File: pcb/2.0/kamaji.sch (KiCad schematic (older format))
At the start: 43 parts, among them J1 RJ10, J2 RJ10, J3 RJ10, J4 RJ10, J5 RJ10, J6 ICSP, J7 USB_B, J8 USB_A, Q1 2N3904, Q2 IRL540N, SW1 SW_Push, SW2 SW_Push, SW3 SW_Push, U1 ATMEGA32U4-AU, Y1 16MHz

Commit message: get gid of 2 nested sheets
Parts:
- added DS1: LCD12864B, kamaji:LCD12864, symbol LCD12864B
- added Q3: IRL540N, TO_SOT_Packages_THT:TO-220-3_Horizontal, symbol IRLIZ44N
- added R20, R25, R26: 10K, symbol R
- added R21, R22, R23, R24: 200R, symbol R
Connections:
- net labels added: DUMMY_EN, LCD_CS, LCD_RST
- no-connect marks 4 -> 6
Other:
- note added: "Dummy load to make sure\npowerbanks don't shut off\npower due to low current"
- note added: "ST7920-based LCD\ndisplay in serial mode"
- moved on the sheet: R8, SW1, SW2, SW3

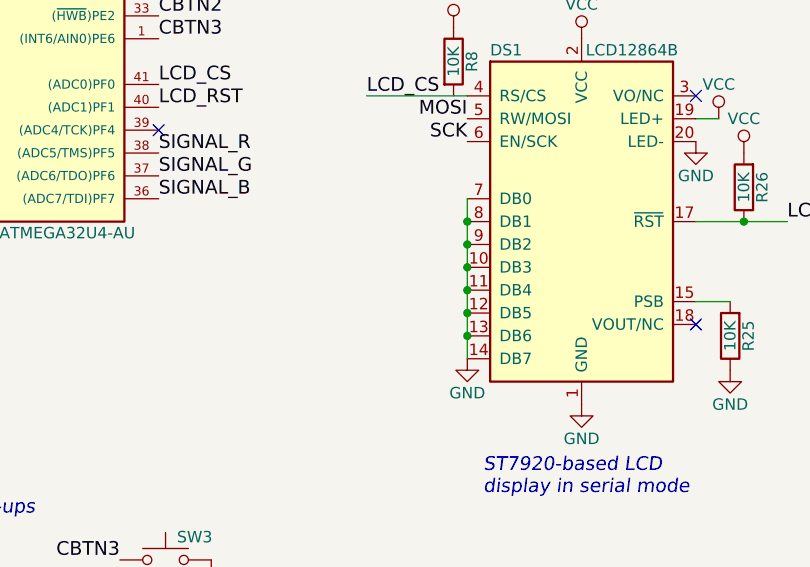
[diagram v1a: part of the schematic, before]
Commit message: minor schamatic changes
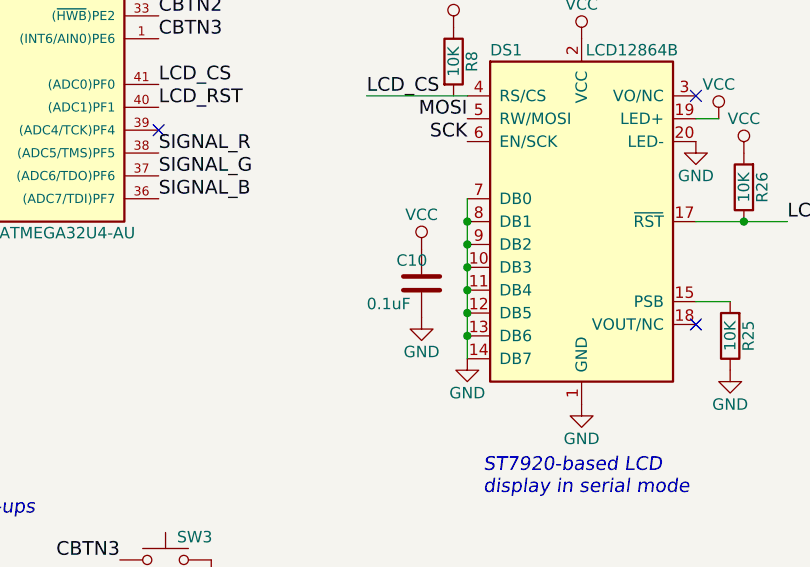
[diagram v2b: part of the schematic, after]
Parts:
- added C10: 0.1uF, symbol C

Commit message: start mapping components to footprints
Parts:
- C1, C10, C2, C3, C4, C5, C6: footprint (none) -> Capacitors_SMD:C_1206_HandSoldering
- J1, J2, J3, J4, J5: footprint (none) -> kamaji:RJ10
- J6: footprint (none) -> Connectors_IDC:IDC-Header_2x03_Pitch2.54mm_Straight
- J7: footprint (none) -> Connectors:USB_B
- J8: footprint (none) -> Connectors:USB_A
- JP1, JP2, JP3: footprint (none) -> Socket_Strips:Socket_Strip_Straight_1x02_Pitch2.54mm
- LS1: footprint (none) -> kamaji:buzzer_30x17
- R1, R10, R11, R12, R13, R14, R15, R2, R20, R21, R22, R23, R24, R25, R26, R3, R4, R5, R6, R7, R8, R9: footprint (none) -> Resistors_SMD:R_1206_HandSoldering

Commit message: finish mapping components to footprints
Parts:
- D1: footprint (none) -> kamaji:LED_RGB_common_cathode_5mm
- F1: footprint (none) -> Resistors_SMD:R_1812_HandSoldering
- RV2: footprint (none) -> kamaji:Potentiometer_Wheel_16mm
- SW1, SW2, SW3: footprint (none) -> Buttons_Switches_THT:SW_PUSH-12mm
- Y1: footprint (none) -> Crystals:Crystal_HC49-U_Vertical
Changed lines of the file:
@@
 F 0 "Y1" H 1300 2130 50  0000 C CNN
 F 1 "16MHz" H 1300 1830 50  0000 C CNN
-F 2 "" H 1300 1980 50  0001 C CNN
+F 2 "Crystals:Crystal_HC49-U_Vertical" H 1300 1980 50  0001 C CNN
 F 3 "" H 1300 1980 50  0001 C CNN
 	1    1300 1980
@@
 F 0 "SW1" H 1400 6060 50  0000 L CNN
 F 1 "SW_Push" H 1350 5900 50  0001 C CNN
-F 2 "" H 1350 6160 50  0001 C CNN
+F 2 "Buttons_Switches_THT:SW_PUSH-12mm" H 1350 6160 50  0001 C CNN
 F 3 "" H 1350 6160 50  0001 C CNN
 	1    1350 5960
@@
 F 0 "SW2" H 2630 6060 50  0000 L CNN
 F 1 "SW_Push" H 2580 5900 50  0001 C CNN
-F 2 "" H 2580 6160 50  0001 C CNN
+F 2 "Buttons_Switches_THT:SW_PUSH-12mm" H 2580 6160 50  0001 C CNN
 F 3 "" H 2580 6160 50  0001 C CNN
 	1    2580 5960
@@
 F 0 "SW3" H 3810 6060 50  0000 L CNN
 F 1 "SW_Push" H 3760 5900 50  0001 C CNN
-F 2 "" H 3760 6160 50  0001 C CNN
+F 2 "Buttons_Switches_THT:SW_PUSH-12mm" H 3760 6160 50  0001 C CNN
 F 3 "" H 3760 6160 50  0001 C CNN
 	1    3760 5960
@@
 F 0 "F1" V 8720 4950 50  0000 C CNN
 F 1 "1A" V 8565 4950 50  0000 C CNN
-F 2 "" V 8570 4950 50  0001 C CNN
+F 2 "Resistors_SMD:R_1812_HandSoldering" V 8570 4950 50  0001 C CNN
 F 3 "" H 8640 4950 50  0001 C CNN
 	1    8640 4950
@@
 F 0 "D1" H 8500 3660 50  0000 C CNN
 F 1 "LED_CRGB" H 8500 2940 50  0000 C CNN
-F 2 "" H 8500 3240 50  0001 C CNN
+F 2 "kamaji:LED_RGB_common_cathode_5mm" H 8500 3240 50  0001 C CNN
 F 3 "" H 8500 3240 50  0001 C CNN
 	1    8500 3290
@@
 F 0 "RV2" V 9870 1710 50  0000 C CNN
 F 1 "VOLUME" V 10070 1720 50  0000 C CNN
-F 2 "" H 9880 1720 50  0001 C CNN
+F 2 "kamaji:Potentiometer_Wheel_16mm" H 9880 1720 50  0001 C CNN
 F 3 "" H 9880 1720 50  0001 C CNN
 	1    9880 1720

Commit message: test point, 6th player socket
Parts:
- removed D1: LED_CRGB, kamaji:LED_RGB_common_cathode_5mm, symbol LED_CRGB
- removed JP1: Jumper, Socket_Strips:Socket_Strip_Straight_1x02_Pitch2.54mm, symbol Jumper
- removed R11, R12: 220R, Resistors_SMD:R_1206_HandSoldering, symbol R
- added J10: TEST_5V, Measurement_Points:Test_Point_2Pads, symbol TEST_2P
- added J6: RJ10, kamaji:RJ10, symbol RJ10
- added J9: TEST_28V, Measurement_Points:Test_Point_2Pads, symbol TEST_2P
- renumbered J6 to ICSP1
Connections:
- net labels added: PBTN6, PLED6
- wire segments 51 -> 52
- no-connect marks 6 -> 4
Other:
- note removed: "Break for current\nmeasurement"
- note removed: "Signal LED"
- moved on the sheet: F1, J1, J2, J3, J4, J5, R4, R5, R6, R7, R9

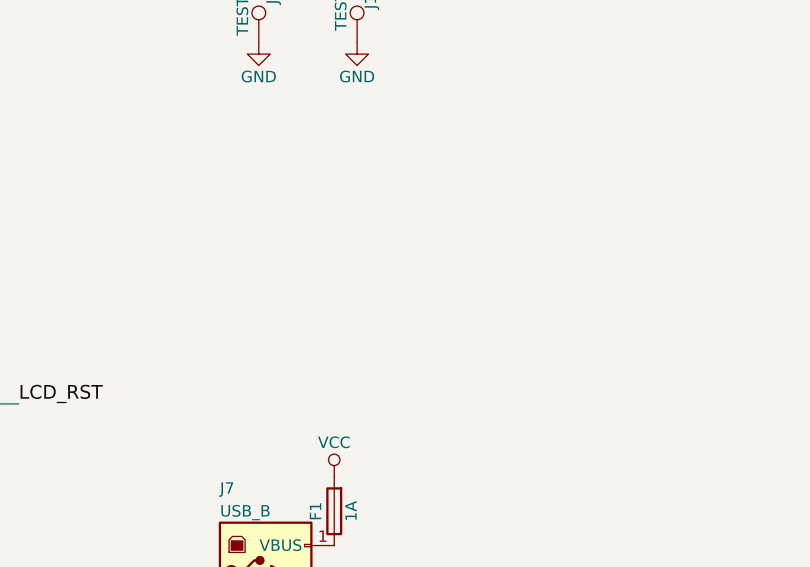
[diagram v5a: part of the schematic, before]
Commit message: place the RJ10 sockets on the PCB
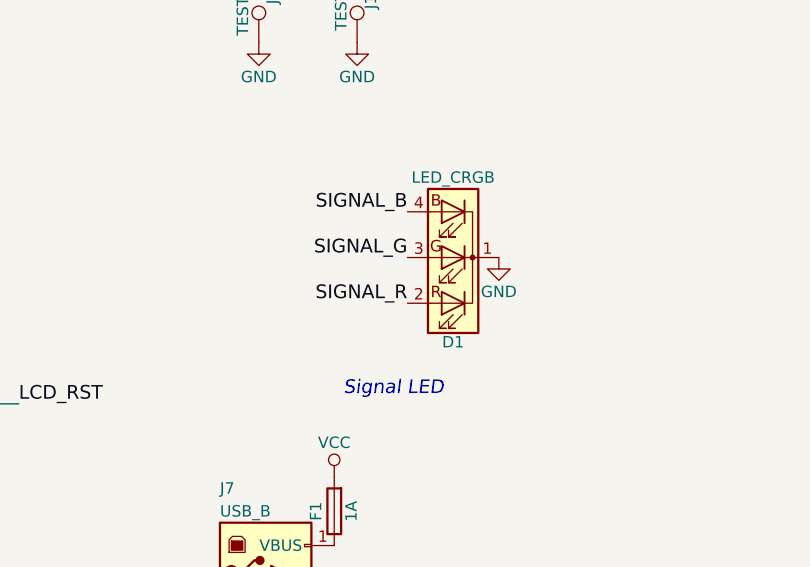
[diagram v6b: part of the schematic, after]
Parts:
- added D1: LED_CRGB, kamaji:LED_RGB_common_cathode_5mm, symbol LED_CRGB
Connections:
- net GND: now also D1.1 (K)
- net SIGNAL_B: now also D1.4 (BA)
- net SIGNAL_G: now also D1.3 (GA)
- net SIGNAL_R: now also D1.2 (RA)
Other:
- note added: "Signal LED"

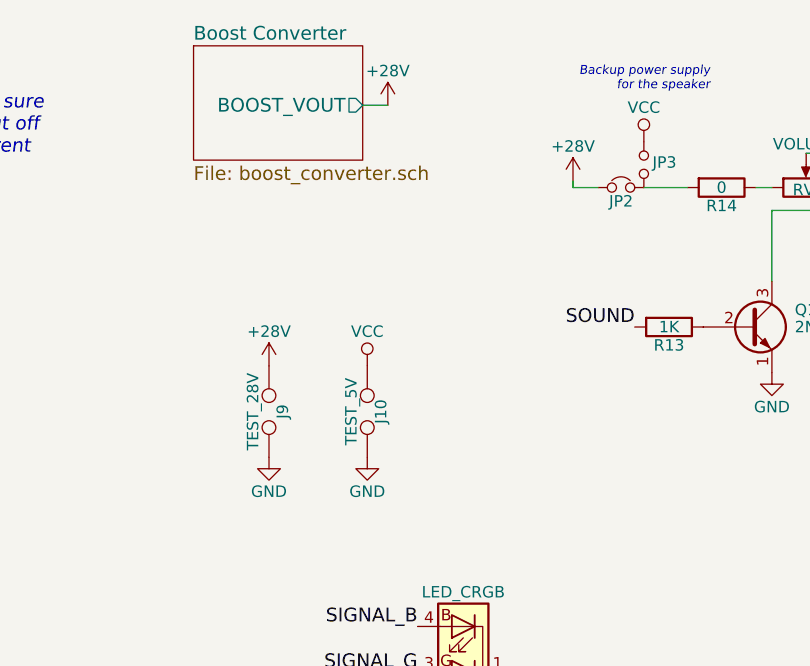
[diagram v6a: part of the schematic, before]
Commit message: roughly place components on the PCB
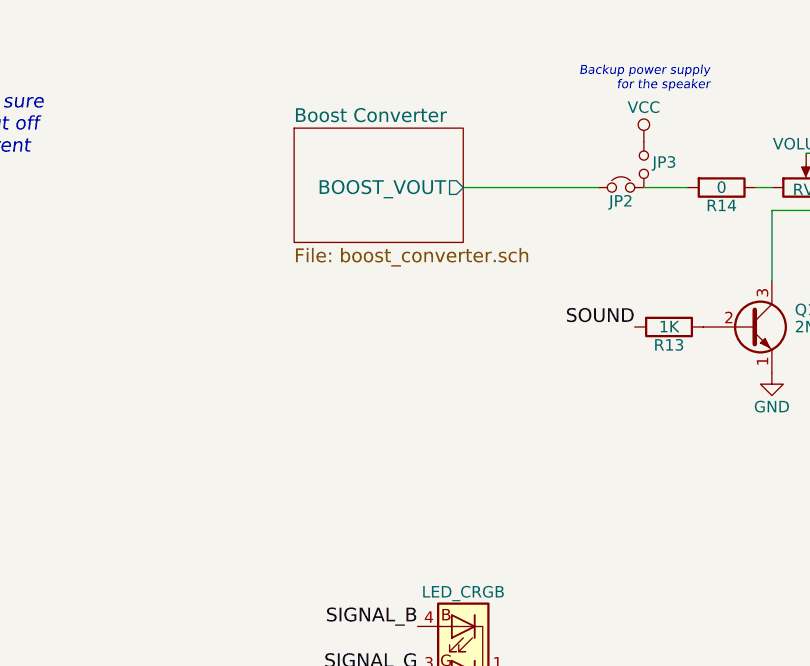
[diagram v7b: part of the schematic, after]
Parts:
- removed J10: TEST_5V, Measurement_Points:Test_Point_2Pads, symbol TEST_2P
- removed J9: TEST_28V, Measurement_Points:Test_Point_2Pads, symbol TEST_2P
- R21, R22, R23, R24: footprint Resistors_SMD:R_1206_HandSoldering -> Resistors_THT:R_Axial_DIN0207_L6.3mm_D2.5mm_P10.16mm_Horizontal
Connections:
- net +28V renamed Boost Converter/BOOST_VOUT
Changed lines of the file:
@@
-	1    0    0    -1
-$EndComp
-$Sheet
-S 7200 1100 740  500
-U 5A30C66D
-F0 "Boost Converter" 60
-F1 "boost_converter.sch" 60
-F2 "BOOST_VOUT" O R 7940 1360 60
-$EndSheet
-$Comp
-L +28V #PWR033
-U 1 1 5A30EB28
-P 8860 1690
-F 0 "#PWR033" H 8860 1540 50  0001 C CNN
-F 1 "+28V" H 8860 1840 50  0000 C CNN
-F 2 "" H 9110 1740 50  0001 C CNN
-F 3 "" H 9110 1740 50  0001 C CNN
-	1    8860 1690
 	1    0    0    -1
 $EndComp
@@
 $EndComp
 $Comp
-L VCC #PWR034
+L VCC #PWR033
 U 1 1 5A3130F9
 P 5020 3630
-F 0 "#PWR034" H 5020 3480 50  0001 C CNN
+F 0 "#PWR033" H 5020 3480 50  0001 C CNN
 F 1 "VCC" H 5020 3780 50  0000 C CNN
 F 2 "" H 5020 3630 50  0001 C CNN
@@
 $EndComp
 $Comp
-L VCC #PWR035
+L VCC #PWR034
 U 1 1 5A31C798
 P 4910 1480
-F 0 "#PWR035" H 4910 1330 50  0001 C CNN
+F 0 "#PWR034" H 4910 1330 50  0001 C CNN
 F 1 "VCC" H 4910 1630 50  0000 C CNN
 F 2 "" H 4910 1480 50  0001 C CNN
@@
 $EndComp
 $Comp
-L GND #PWR036
+L GND #PWR035
 U 1 1 5A31CC00
 P 4910 1680
-F 0 "#PWR036" H 4910 1430 50  0001 C CNN
+F 0 "#PWR035" H 4910 1430 50  0001 C CNN
 F 1 "GND" H 4910 1530 50  0000 C CNN
 F 2 "" H 4910 1680 50  0001 C CNN
@@
 $EndComp
 $Comp
-L GND #PWR037
+L GND #PWR036
 U 1 1 5A31EA2B
 P 9730 2530
-F 0 "#PWR037" H 9730 2280 50  0001 C CNN
+F 0 "#PWR036" H 9730 2280 50  0001 C CNN
 F 1 "GND" H 9730 2380 50  0000 C CNN
 F 2 "" H 9730 2530 50  0001 C CNN
@@
 $EndComp
 $Comp
-L VCC #PWR038
+L VCC #PWR037
 U 1 1 5A317FA1
 P 9170 1520
-F 0 "#PWR038" H 9170 1370 50  0001 C CNN
+F 0 "#PWR037" H 9170 1370 50  0001 C CNN
 F 1 "VCC" H 9170 1670 50  0000 C CNN
 F 2 "" H 9170 1520 50  0001 C CNN
@@
 Backup power supply\nfor the speaker
 $Comp
-L +28V #PWR039
-U 1 1 5A33C3C6
-P 8050 1360
-F 0 "#PWR039" H 8050 1210 50  0001 C CNN
-F 1 "+28V" H 8050 1510 50  0000 C CNN
-F 2 "" H 8300 1410 50  0001 C CNN
-F 3 "" H 8300 1410 50  0001 C CNN
-	1    8050 1360
-	1    0    0    -1
-$EndComp
-$Comp
 L POT RV2
 U 1 1 5A34230D
@@
 F 0 "R21" V 5690 1970 50  0000 C CNN
 F 1 "200R" V 5610 1970 50  0000 C CNN
-F 2 "Resistors_SMD:R_1206_HandSoldering" V 5540 1970 50  0001 C CNN
+F 2 "Resistors_THT:R_Axial_DIN0207_L6.3mm_D2.5mm_P10.16mm_Horizontal" V 5540 1970 50  0001 C CNN
 F 3 "" H 5610 1970 50  0001 C CNN
 	1    5610 1970
@@
 F 0 "R24" V 6200 1970 50  0000 C CNN
 F 1 "200R" V 6120 1970 50  0000 C CNN
-F 2 "Resistors_SMD:R_1206_HandSoldering" V 6050 1970 50  0001 C CNN
+F 2 "Resistors_THT:R_Axial_DIN0207_L6.3mm_D2.5mm_P10.16mm_Horizontal" V 6050 1970 50  0001 C CNN
 F 3 "" H 6120 1970 50  0001 C CNN
 	1    6120 1970
@@
 F 0 "R22" V 5860 1970 50  0000 C CNN
 F 1 "200R" V 5780 1970 50  0000 C CNN
-F 2 "Resistors_SMD:R_1206_HandSoldering" V 5710 1970 50  0001 C CNN
+F 2 "Resistors_THT:R_Axial_DIN0207_L6.3mm_D2.5mm_P10.16mm_Horizontal" V 5710 1970 50  0001 C CNN
 F 3 "" H 5780 1970 50  0001 C CNN
 	1    5780 1970
@@
 Dummy load to make sure\npowerbanks don't shut off\npower due to low current
 $Comp
-L GND #PWR040
+L GND #PWR038
 U 1 1 5A350150
 P 5860 2520
-F 0 "#PWR040" H 5860 2270 50  0001 C CNN
+F 0 "#PWR038" H 5860 2270 50  0001 C CNN
 F 1 "GND" H 5860 2370 50  0000 C CNN
 F 2 "" H 5860 2520 50  0001 C CNN
@@
 $EndComp
 $Comp
-L GND #PWR041
+L GND #PWR039
 U 1 1 5A350156
 P 5560 2620
-F 0 "#PWR041" H 5560 2370 50  0001 C CNN
+F 0 "#PWR039" H 5560 2370 50  0001 C CNN
 F 1 "GND" H 5560 2470 50  0000 C CNN
 F 2 "" H 5560 2620 50  0001 C CNN
@@
 $EndComp
 $Comp
-L VCC #PWR042
+L VCC #PWR040
 U 1 1 5A35016A
 P 5860 1820
-F 0 "#PWR042" H 5860 1670 50  0001 C CNN
+F 0 "#PWR040" H 5860 1670 50  0001 C CNN
 F 1 "VCC" H 5860 1970 50  0000 C CNN
 F 2 "" H 5860 1820 50  0001 C CNN
@@
 F 0 "R23" V 6030 1970 50  0000 C CNN
 F 1 "200R" V 5950 1970 50  0000 C CNN
-F 2 "Resistors_SMD:R_1206_HandSoldering" V 5880 1970 50  0001 C CNN
+F 2 "Resistors_THT:R_Axial_DIN0207_L6.3mm_D2.5mm_P10.16mm_Horizontal" V 5880 1970 50  0001 C CNN
 F 3 "" H 5950 1970 50  0001 C CNN
 	1    5950 1970
@@
 $EndComp
 $Comp
-L GND #PWR043
+L GND #PWR041
 U 1 1 5A352FCB
 P 5580 5280
-F 0 "#PWR043" H 5580 5030 50  0001 C CNN
+F 0 "#PWR041" H 5580 5030 50  0001 C CNN
 F 1 "GND" H 5580 5130 50  0000 C CNN
 F 2 "" H 5580 5280 50  0001 C CNN
@@
 $EndComp
 $Comp
-L VCC #PWR044
+L VCC #PWR042
 U 1 1 5A352FD1
 P 5580 3680
-F 0 "#PWR044" H 5580 3530 50  0001 C CNN
+F 0 "#PWR042" H 5580 3530 50  0001 C CNN
 F 1 "VCC" H 5580 3830 50  0000 C CNN
 F 2 "" H 5580 3680 50  0001 C CNN
@@
 NoConn ~ 6080 3930
 $Comp
-L VCC #PWR045
+L VCC #PWR043
 U 1 1 5A352FDF
 P 6180 4030
-F 0 "#PWR045" H 6180 3880 50  0001 C CNN
+F 0 "#PWR043" H 6180 3880 50  0001 C CNN
 F 1 "VCC" H 6180 4180 50  0000 C CNN
 F 2 "" H 6180 4030 50  0001 C CNN
@@
 $EndComp
 $Comp
-L GND #PWR046
+L GND #PWR044
 U 1 1 5A352FE6
 P 6080 4130
-F 0 "#PWR046" H 6080 3880 50  0001 C CNN
+F 0 "#PWR044" H 6080 3880 50  0001 C CNN
 F 1 "GND" H 6080 3980 50  0000 C CNN
 F 2 "" H 6080 4130 50  0001 C CNN
@@
 $EndComp
 $Comp
-L VCC #PWR047
+L VCC #PWR045
 U 1 1 5A352FEC
 P 6290 4180
-F 0 "#PWR047" H 6290 4030 50  0001 C CNN
+F 0 "#PWR045" H 6290 4030 50  0001 C CNN
 F 1 "VCC" H 6290 4330 50  0000 C CNN
 F 2 "" H 6290 4180 50  0001 C CNN
@@
 $EndComp
 $Comp
-L GND #PWR048
+L GND #PWR046
 U 1 1 5A353001
 P 6230 5130
-F 0 "#PWR048" H 6230 4880 50  0001 C CNN
+F 0 "#PWR046" H 6230 4880 50  0001 C CNN
 F 1 "GND" H 6230 4980 50  0000 C CNN
 F 2 "" H 6230 5130 50  0001 C CNN
@@
 ST7920-based LCD\ndisplay in serial mode
 $Comp
-L GND #PWR049
+L GND #PWR047
 U 1 1 5A35300B
 P 5080 5080
-F 0 "#PWR049" H 5080 4830 50  0001 C CNN
+F 0 "#PWR047" H 5080 4830 50  0001 C CNN
 F 1 "GND" H 5080 4930 50  0000 C CNN
 F 2 "" H 5080 5080 50  0001 C CNN
@@
 $EndComp
 $Comp
-L GND #PWR050
+L GND #PWR048
 U 1 1 5A35018A
 P 4880 4900
-F 0 "#PWR050" H 4880 4650 50  0001 C CNN
+F 0 "#PWR048" H 4880 4650 50  0001 C CNN
 F 1 "GND" H 4880 4750 50  0000 C CNN
 F 2 "" H 4880 4900 50  0001 C CNN
@@
 $EndComp
 $Comp
-L VCC #PWR051
+L VCC #PWR049
 U 1 1 5A350190
 P 4880 4600
-F 0 "#PWR051" H 4880 4450 50  0001 C CNN
+F 0 "#PWR049" H 4880 4450 50  0001 C CNN
 F 1 "VCC" H 4880 4750 50  0000 C CNN
 F 2 "" H 4880 4600 50  0001 C CNN
@@
 SIGNAL_B
 $Comp
-L GND #PWR052
+L GND #PWR050
 U 1 1 5A3A8D7F
 P 6320 7000
-F 0 "#PWR052" H 6320 6750 50  0001 C CNN
+F 0 "#PWR050" H 6320 6750 50  0001 C CNN
 F 1 "GND" H 6320 6850 50  0000 C CNN
 F 2 "" H 6320 7000 50  0001 C CNN
@@
 $EndComp
 $Comp
-L GND #PWR053
+L GND #PWR051
 U 1 1 5A3A8D85
 P 6120 7000
-F 0 "#PWR053" H 6120 6750 50  0001 C CNN
+F 0 "#PWR051" H 6120 6750 50  0001 C CNN
 F 1 "GND" H 6120 6850 50  0000 C CNN
 F 2 "" H 6120 7000 50  0001 C CNN
@@
 Text Label 3730 3180 0    60   ~ 0
 PLED6
-$Comp
-L TEST_2P J9
-U 1 1 5A3AAF62
-P 7530 2700
-F 0 "J9" H 7530 2760 50  0000 C CNN
-F 1 "TEST_28V" H 7530 2630 50  0000 C CNN
-F 2 "Measurement_Points:Test_Point_2Pads" H 7530 2700 50  0001 C CNN
-F 3 "" H 7530 2700 50  0001 C CNN
-	1    7530 2700
-	0    1    1    0
-$EndComp
-$Comp
-L +28V #PWR054
-U 1 1 5A3AB05D
-P 7530 2500
-F 0 "#PWR054" H 7530 2350 50  0001 C CNN
-F 1 "+28V" H 7530 2650 50  0000 C CNN
-F 2 "" H 7780 2550 50  0001 C CNN
-F 3 "" H 7780 2550 50  0001 C CNN
-	1    7530 2500
-	1    0    0    -1
-$EndComp
-$Comp
-L GND #PWR055
-U 1 1 5A3AB146
-P 7530 2900
-F 0 "#PWR055" H 7530 2650 50  0001 C CNN
-F 1 "GND" H 7530 2750 50  0000 C CNN
-F 2 "" H 7530 2900 50  0001 C CNN
-F 3 "" H 7530 2900 50  0001 C CNN
-	1    7530 2900
-	1    0    0    -1
-$EndComp
-$Comp
-L TEST_2P J10
-U 1 1 5A3AB726
-P 7960 2700
-F 0 "J10" H 7960 2760 50  0000 C CNN
-F 1 "TEST_5V" H 7960 2630 50  0000 C CNN
-F 2 "Measurement_Points:Test_Point_2Pads" H 7960 2700 50  0001 C CNN
-F 3 "" H 7960 2700 50  0001 C CNN
-	1    7960 2700
-	0    1    1    0
-$EndComp
-$Comp
-L VCC #PWR056
-U 1 1 5A3AB8AB
-P 7960 2500
-F 0 "#PWR056" H 7960 2350 50  0001 C CNN
-F 1 "VCC" H 7960 2650 50  0000 C CNN
-F 2 "" H 7960 2500 50  0001 C CNN
-F 3 "" H 7960 2500 50  0001 C CNN
-	1    7960 2500
-	1    0    0    -1
-$EndComp
-$Comp
-L GND #PWR057
-U 1 1 5A3AB95B
-P 7960 2900
-F 0 "#PWR057" H 7960 2650 50  0001 C CNN
-F 1 "GND" H 7960 2750 50  0000 C CNN
-F 2 "" H 7960 2900 50  0001 C CNN
-F 3 "" H 7960 2900 50  0001 C CNN
-	1    7960 2900
-	1    0    0    -1
-$EndComp
 Wire Wire Line
 	2180 1230 2880 1230
@@
 Wire Wire Line
 	4820 7040 4920 7040
-Wire Wire Line
-	7940 1360 8050 1360
-Wire Wire Line
-	8970 1720 8860 1720
-Wire Wire Line
-	8860 1720 8860 1690
 Wire Wire Line
 	9880 1570 10030 1570
@@
 Signal LED
 $Comp
-L GND #PWR058
+L GND #PWR052
 U 1 1 5A3ACD5F
 P 8580 3840
-F 0 "#PWR058" H 8580 3590 50  0001 C CNN
+F 0 "#PWR052" H 8580 3590 50  0001 C CNN
 F 1 "GND" H 8580 3690 50  0000 C CNN
 F 2 "" H 8580 3840 50  0001 C CNN
@@
 Text Label 8180 3640 2    60   ~ 0
 SIGNAL_B
+$Sheet
+S 7640 1460 740  500
+U 5A30C66D
+F0 "Boost Converter" 60
+F1 "boost_converter.sch" 60
+F2 "BOOST_VOUT" O R 8380 1720 60
+$EndSheet
+Wire Wire Line
+	8380 1720 8970 1720
 $EndSCHEMATC
